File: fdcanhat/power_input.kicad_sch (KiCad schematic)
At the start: 14 parts, among them J2 XT30 M, J3 XT30 M, Q1 NMOS, U3 LM74700, U4 INA180

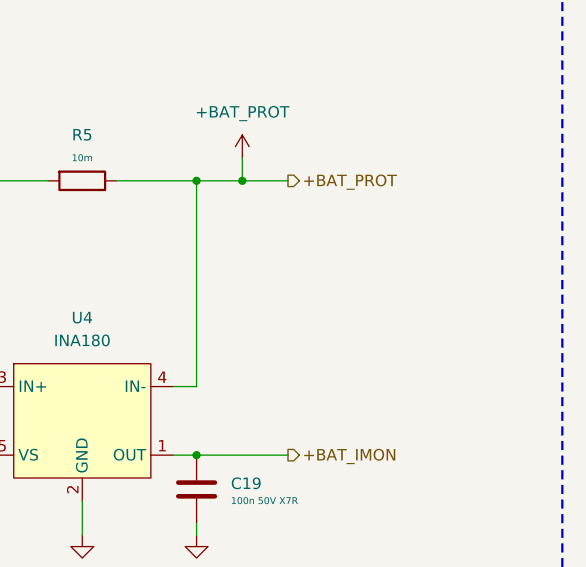
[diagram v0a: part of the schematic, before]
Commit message: ish done with schematics
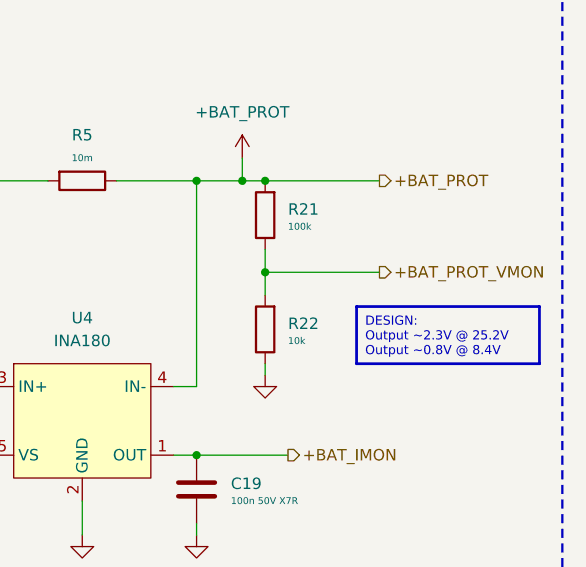
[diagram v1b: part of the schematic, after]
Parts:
- added R21: 100k, symbol Device:R
- added R22: 10k, symbol Device:R
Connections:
- net +BAT_PROT: now also R21.2
- net GND: now also R22.1
- new net +BAT_PROT_VMON: R21.1, R22.2

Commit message: board layout done, ready for routing
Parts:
- removed J3: XT30 M, symbol 0_connectors:Conn_01x02_Mounting
- C1: renamed from C13; footprint (none) -> 0_capacitor_smd:C_0402_1005Metric; LCSC (none) -> C307331
- C2: renamed from C14; value 1u 50V X7R -> 1u 50V X5R; footprint (none) -> 0_capacitor_smd:C_0603_1608Metric; LCSC (none) -> C15849
- C3: renamed from C15; value 10u 50V X7R -> 10u 50V X5R; footprint (none) -> 0_capacitor_smd:C_0805_2012Metric; LCSC (none) -> C440198
- C4: renamed from C16; value 10u 50V X7R -> 10u 50V X5R; footprint (none) -> 0_capacitor_smd:C_0805_2012Metric; LCSC (none) -> C440198
- C5: renamed from C17; value 10u 50V X7R -> 10u 50V X5R; footprint (none) -> 0_capacitor_smd:C_0805_2012Metric; LCSC (none) -> C440198
- C6: renamed from C18; footprint (none) -> 0_capacitor_smd:C_0402_1005Metric; LCSC (none) -> C307331
- C7: renamed from C19; footprint (none) -> 0_capacitor_smd:C_0402_1005Metric; LCSC (none) -> C307331
- D1: footprint (none) -> Diode_SMD:D_SMB; LCSC (none) -> C19077583
- J3: renamed from J2; footprint (none) -> 0_connectors:XT30PW-M; now left out of the parts list
- Q1: footprint (none) -> 0_transistors:DFN-8; LCSC (none) -> C467174
- R1: renamed from R5; footprint (none) -> 0_resistor_smd:R_2512_6332Metric; LCSC (none) -> C108943
- R2: renamed from R21; footprint (none) -> 0_resistor_smd:R_0402_1005Metric; LCSC (none) -> C25741
- R3: renamed from R22; footprint (none) -> 0_resistor_smd:R_0402_1005Metric; LCSC (none) -> C25744
- renumbered U3 to U1, U4 to U2
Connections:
- net ID_VCAP: now reaches C2.2, U1.1 (VCAP)
- no-connect marks 4 -> 2

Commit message: almost done
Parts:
- removed C4, C5: 10u 50V X5R, 0_capacitor_smd:C_0805_2012Metric, symbol Device:C
- removed Q1: NMOS, 0_transistors:DFN-8, symbol Simulation_SPICE:NMOS
- removed U1: LM74700, 0_power:SOT-23-6, symbol 0_power:LM74700
- added D1: MBR1060CS, 0_diodes:TO-252-2_L6.6-W6.1-P4.57-LS10.2-TR-CW, symbol Device:D_Schottky_Dual_CommonCathode_AKA_Parallel
- C2: value 1u 50V X5R -> 10u 50V X5R; footprint 0_capacitor_smd:C_0603_1608Metric -> 0_capacitor_smd:C_0805_2012Metric; LCSC C15849 -> C440198
- renumbered C6 to C4, C7 to C5, D1 to D2, U2 to U1
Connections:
- net ID_VCAP is gone; now on net GND: C2.2
- net +BAT: now also J3.2 (Pin_2), D1.1 (A), D1.3 (A); no longer C2.1, J3.1 (Pin_1)
- net +BAT_PROT_PRE_MEAS: now also C2.1, D1.2 (K)
- net GND: now also J3.1 (Pin_1); no longer J3.2 (Pin_2)
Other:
- moved on the sheet: C1, D2, J3

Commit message: done doublechecking, going for review
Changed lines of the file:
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@@
+		)
+	)
+	(text_box "DESIGN:\nV_SENSE @ 5A = 50 mV\nVOUT = 20 * 0.05 = 1.0 V"
+		(exclude_from_sim no)
+		(at 236.22 121.92 0)
+		(size 25.4 6.35)
+		(margins 0.9525 0.9525 0.9525 0.9525)
+		(stroke
+			(width 0.3048)
+			(type solid)
+			(color 132 132 132 1)
+		)
+		(fill
+			(type none)
+		)
+		(effects
+			(font
+				(face "KiCad Font")
+				(size 1.016 1.016)
+			)
+			(justify left top)
 		)
 	)

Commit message: ready for last scrut
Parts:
- removed C5: 100n 50V X7R, 0_capacitor_smd:C_0402_1005Metric, symbol Device:C
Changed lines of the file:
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@@
-	)
-	(junction
-		(at 229.87 114.3)
-		(diameter 0)
-		(color 0 0 0 0)
 	)
 	(junction
@@
 	(wire
 		(pts
-			(xy 227.33 114.3) (xy 229.87 114.3)
+			(xy 227.33 114.3) (xy 240.03 114.3)
 		)
 		(stroke
@@
 	(wire
 		(pts
-			(xy 229.87 114.3) (xy 240.03 114.3)
-		)
-		(stroke
-			(width 0)
-			(type default)
-		)
-	)
-	(wire
-		(pts
 			(xy 237.49 91.44) (xy 237.49 93.98)
 		)
@@
 		(pts
 			(xy 195.58 83.82) (xy 204.47 83.82)
-		)
-		(stroke
-			(width 0)
-			(type default)
-		)
-	)
-	(wire
-		(pts
-			(xy 229.87 121.92) (xy 229.87 123.19)
 		)
 		(stroke
@@
 	)
 	(symbol
-		(lib_id "Device:C")
-		(at 229.87 118.11 0)
-		(unit 1)
-		(exclude_from_sim no)
-		(in_bom yes)
-		(on_board yes)
-		(dnp no)
-		(fields_autoplaced yes)
-		(property "Reference" "C5"
-			(at 233.68 117.4749 0)
-			(effects
-				(font
-					(size 1.27 1.27)
-				)
-				(justify left)
-			)
-		)
-		(property "Value" "100n 50V X7R"
-			(at 233.68 119.38 0)
-			(effects
-				(font
-					(size 0.762 0.762)
-				)
-				(justify left)
-			)
-		)
-		(property "Footprint" "0_capacitor_smd:C_0402_1005Metric"
-			(at 230.8352 121.92 0)
-			(effects
-				(font
-					(size 1.27 1.27)
-				)
-				(hide yes)
-			)
-		)
-		(property "Datasheet" "~"
-			(at 229.87 118.11 0)
-			(effects
-				(font
-					(size 1.27 1.27)
-				)
-				(hide yes)
-			)
-		)
-		(property "Description" "Unpolarized capacitor"
-			(at 229.87 118.11 0)
-			(effects
-				(font
-					(size 1.27 1.27)
-				)
-				(hide yes)
-			)
-		)
-		(property "LCSC" "C307331"
-			(at 229.87 118.11 0)
-			(effects
-				(font
-					(size 1.27 1.27)
-				)
-				(hide yes)
-			)
-		)
-		(property "Name" ""
-			(at 229.87 118.11 0)
-			(effects
-				(font
-					(size 1.27 1.27)
-				)
-				(hide yes)
-			)
-		)
-		(pin "1"
-		)
-		(pin "2"
-		)
-		(instances
-			(project "fdcanhat"
-				(path "/4375c315-c696-43df-ab5b-868bd3f1287b/941260c8-26ec-48be-94c9-c4722689d865"
-					(reference "C5")
-					(unit 1)
-				)
-			)
-		)
-	)
-	(symbol
 		(lib_id "0_power:INA180")
 		(at 217.17 111.76 0)
@@
 					(unit 1)
 				)
-			)
-		)
-	)
-	(symbol
-		(lib_id "power:GND")
-		(at 229.87 123.19 0)
-		(unit 1)
-		(exclude_from_sim no)
-		(in_bom yes)
-		(on_board yes)
-		(dnp no)
-		(fields_autoplaced yes)
-		(property "Reference" "#PWR019"
-			(at 229.87 129.54 0)
-			(effects
-				(font
-					(size 1.27 1.27)
-				)
-				(hide yes)
-			)
-		)
-		(property "Value" "GND"
-			(at 229.87 128.27 0)
-			(effects
-				(font
-					(size 1.27 1.27)
-				)
-				(hide yes)
-			)
-		)
-		(property "Footprint" ""
-			(at 229.87 123.19 0)
-			(effects
-				(font
-					(size 1.27 1.27)
-				)
-				(hide yes)
-			)
-		)
-		(property "Datasheet" ""
-			(at 229.87 123.19 0)
-			(effects
-				(font
-					(size 1.27 1.27)
-				)
-				(hide yes)
-			)
-		)
-		(property "Description" "Power symbol creates a global label with name \"GND\" , ground"
-			(at 229.87 123.19 0)
-			(effects
-				(font
-					(size 1.27 1.27)
-				)
-				(hide yes)
-			)
-		)
-		(pin "1"
-		)
-		(instances
-			(project "fdcanhat"
-				(path "/4375c315-c696-43df-ab5b-868bd3f1287b/941260c8-26ec-48be-94c9-c4722689d865"
-					(reference "#PWR019")
-					(unit 1)
-				)
